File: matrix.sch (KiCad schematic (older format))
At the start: 129 parts

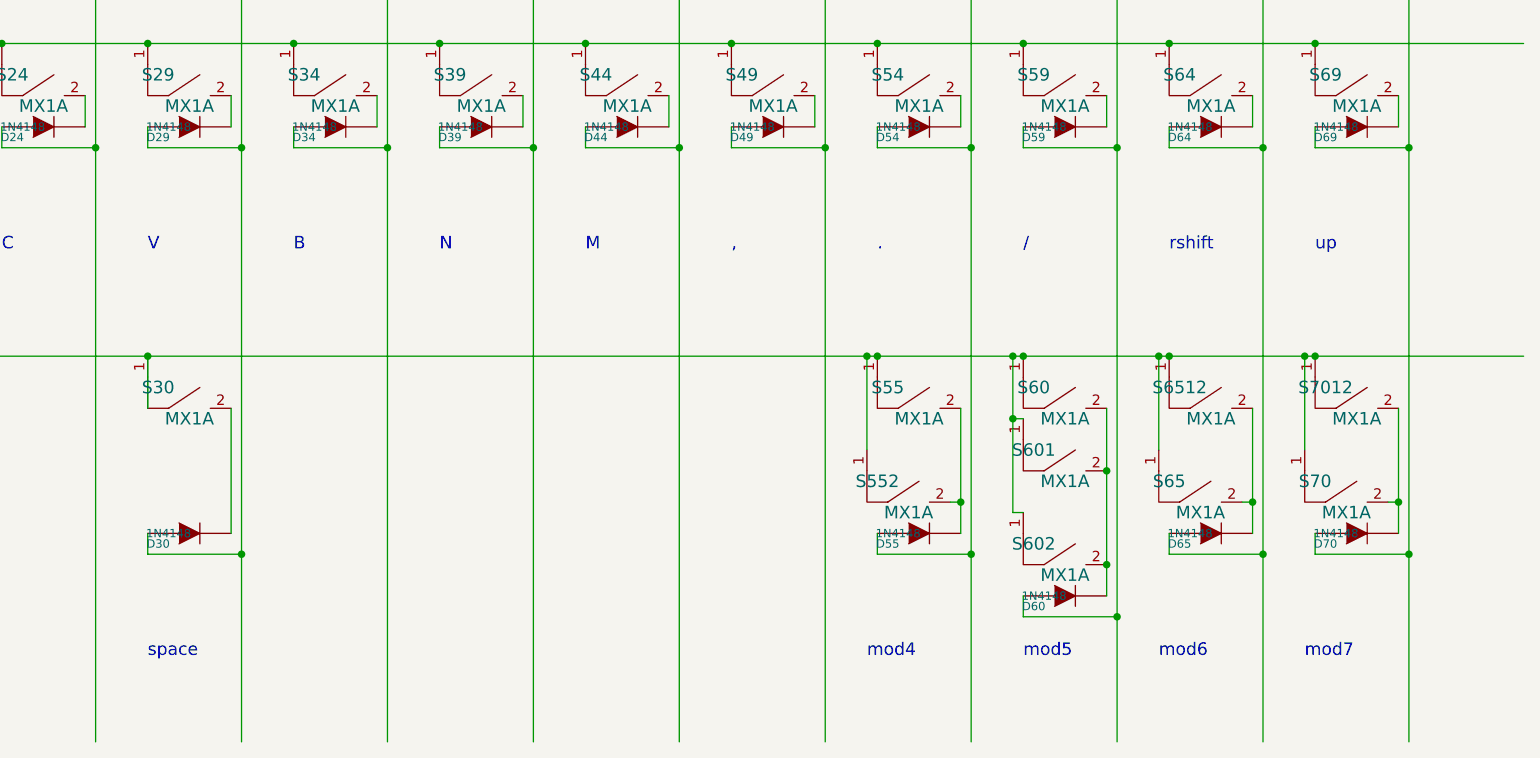
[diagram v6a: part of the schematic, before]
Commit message: New PCB layout for bottom, left, mod4, mod5 and mod6
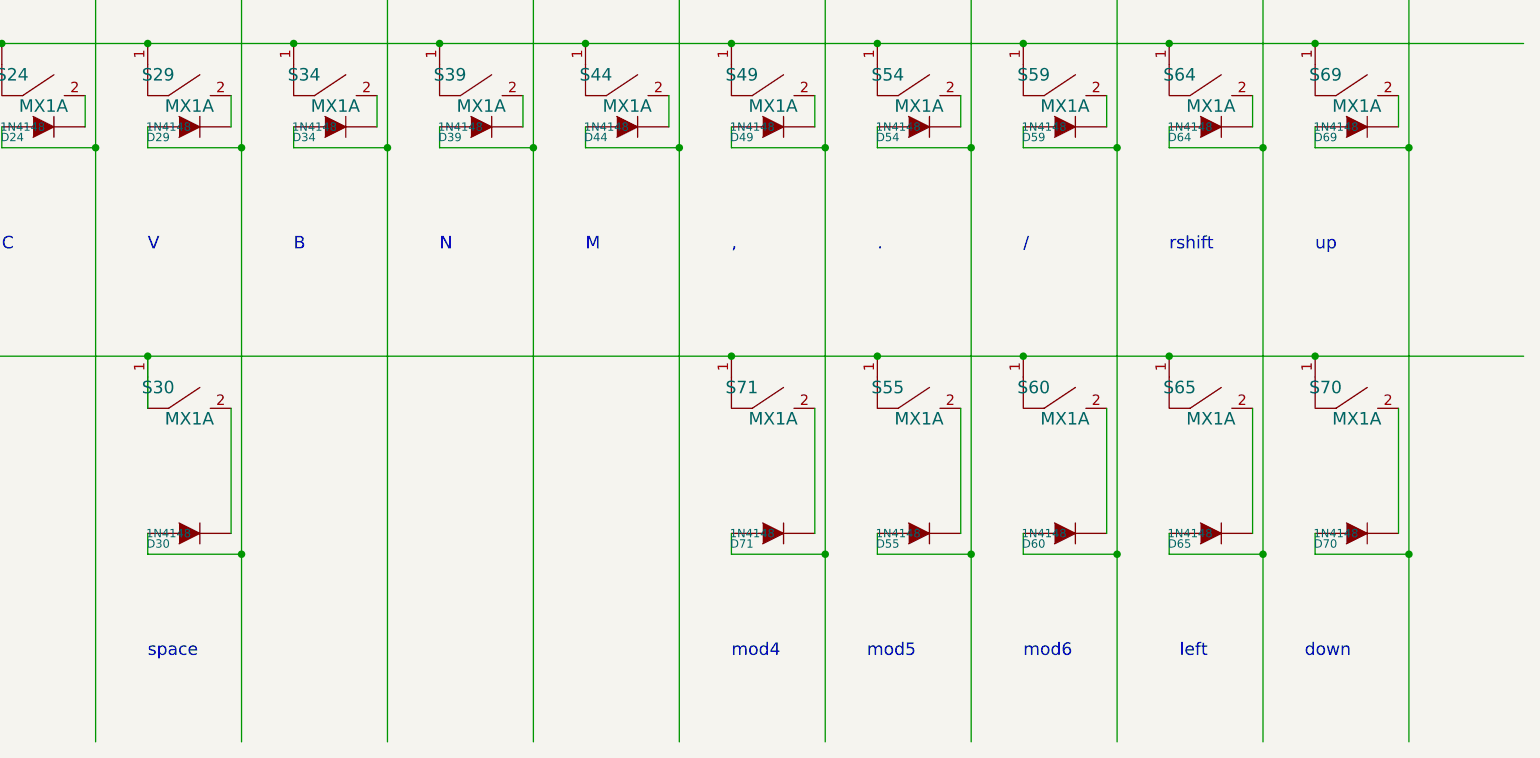
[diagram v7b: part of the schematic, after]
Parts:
- removed S552, S601, S602, S6512, S7012: MX1A, mx1a:MX1A_no3d, symbol mx1a-simple:MX1A
- added D71: 1N4148, 0805:0805D, symbol device:DIODE
- added S71: MX1A, mx1a:MX1A, symbol mx1a-simple:MX1A
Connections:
- wire segments 349 -> 335
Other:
- note added: "down"
- note added: "left"
- note removed: "mod7"
- moved on the sheet: D60, S65, S70
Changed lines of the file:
@@
 L mx1a-simple:MX1A S65
 U 1 1 5040DF5F
-P 11700 9000
-F 0 "S65" H 11550 9250 60  0000 C CNN
-F 1 "MX1A" H 11700 9100 60  0000 C CNN
-F 2 "mx1a:MX1A" H 11700 9000 60  0001 C CNN
-F 3 "" H 11700 9000 60  0001 C CNN
-	1    11700 9000
+P 11750 8550
+F 0 "S65" H 11600 8800 60  0000 C CNN
+F 1 "MX1A" H 11750 8650 60  0000 C CNN
+F 2 "mx1a:MX1A" H 11750 8550 60  0001 C CNN
+F 3 "" H 11750 8550 60  0001 C CNN
+	1    11750 8550
 	1    0    0    -1
 $EndComp
@@
 L mx1a-simple:MX1A S70
 U 1 1 5040DF65
-P 12400 9000
-F 0 "S70" H 12250 9250 60  0000 C CNN
-F 1 "MX1A" H 12400 9100 60  0000 C CNN
-F 2 "mx1a:MX1A" H 12400 9000 60  0001 C CNN
-F 3 "" H 12400 9000 60  0001 C CNN
-	1    12400 9000
-	1    0    0    -1
-$EndComp
-$Comp
-L mx1a-simple:MX1A S552
-U 1 1 5040F08D
-P 10300 9000
-F 0 "S552" H 10150 9250 60  0000 C CNN
-F 1 "MX1A" H 10300 9100 60  0000 C CNN
-F 2 "mx1a:MX1A_no3d" H 10300 9000 60  0001 C CNN
-F 3 "" H 10300 9000 60  0001 C CNN
-	1    10300 9000
-	1    0    0    -1
-$EndComp
-$Comp
-L mx1a-simple:MX1A S602
-U 1 1 5040F09E
-P 11050 9300
-F 0 "S602" H 10900 9550 60  0000 C CNN
-F 1 "MX1A" H 11050 9400 60  0000 C CNN
-F 2 "mx1a:MX1A_no3d" H 11050 9300 60  0001 C CNN
-F 3 "" H 11050 9300 60  0001 C CNN
-	1    11050 9300
-	1    0    0    -1
-$EndComp
-$Comp
-L mx1a-simple:MX1A S6512
-U 1 1 5040F1A3
-P 11750 8550
-F 0 "S6512" H 11600 8800 60  0000 C CNN
-F 1 "MX1A" H 11750 8650 60  0000 C CNN
-F 2 "mx1a:MX1A_no3d" H 11750 8550 60  0001 C CNN
-F 3 "" H 11750 8550 60  0001 C CNN
-	1    11750 8550
-	1    0    0    -1
-$EndComp
-$Comp
-L mx1a-simple:MX1A S7012
-U 1 1 5040F1FA
 P 12450 8550
-F 0 "S7012" H 12300 8800 60  0000 C CNN
+F 0 "S70" H 12300 8800 60  0000 C CNN
 F 1 "MX1A" H 12450 8650 60  0000 C CNN
-F 2 "mx1a:MX1A_no3d" H 12450 8550 60  0001 C CNN
+F 2 "mx1a:MX1A" H 12450 8550 60  0001 C CNN
 F 3 "" H 12450 8550 60  0001 C CNN
 	1    12450 8550
@@
 L device:DIODE D60
 U 1 1 506B59FB
-P 11050 9300
-F 0 "D60" H 10900 9250 40  0000 C CNN
-F 1 "1N4148" H 10950 9300 40  0000 C CNN
-F 2 "0805:0805D" H 11050 9300 60  0001 C CNN
-F 3 "" H 11050 9300 60  0001 C CNN
-F 4 "DC Components" H 5000 5050 60  0001 C CNN "Vendor"
-F 5 "CD4148WS(0805C)" H 5000 5050 60  0001 C CNN "Product"
-F 6 "TME" H 5000 5050 60  0001 C CNN "Supplier"
-F 7 "1N4148-0805" H 5000 5050 60  0001 C CNN "Supplier Symbol"
-	1    11050 9300
+P 11050 9000
+F 0 "D60" H 10900 8950 40  0000 C CNN
+F 1 "1N4148" H 10950 9000 40  0000 C CNN
+F 2 "0805:0805D" H 11050 9000 60  0001 C CNN
+F 3 "" H 11050 9000 60  0001 C CNN
+F 4 "DC Components" H 5000 4750 60  0001 C CNN "Vendor"
+F 5 "CD4148WS(0805C)" H 5000 4750 60  0001 C CNN "Product"
+F 6 "TME" H 5000 4750 60  0001 C CNN "Supplier"
+F 7 "1N4148-0805" H 5000 4750 60  0001 C CNN "Supplier Symbol"
+	1    11050 9000
 	1    0    0    -1
 $EndComp
@@
 F 7 "1N4148-0805" H 3350 3900 60  0001 C CNN "Supplier Symbol"
 	1    3350 5550
-	1    0    0    -1
-$EndComp
-$Comp
-L mx1a-simple:MX1A S601
-U 1 1 5040F098
-P 11050 8850
-F 0 "S601" H 10900 9100 60  0000 C CNN
-F 1 "MX1A" H 11050 8950 60  0000 C CNN
-F 2 "mx1a:MX1A_no3d" H 11050 8850 60  0001 C CNN
-F 3 "" H 11050 8850 60  0001 C CNN
-	1    11050 8850
 	1    0    0    -1
 $EndComp
@@
 mod3
 Text Notes 10100 9600 0    60   ~ 0
-mod4
+mod5
 Text Notes 10850 9600 0    60   ~ 0
-mod5
-Text Notes 11500 9600 0    60   ~ 0
 mod6
+Text Notes 11600 9600 0    60   ~ 0
+left
 Text Notes 12200 9600 0    60   ~ 0
-mod7
+down
 Wire Wire Line
 	4300 1400 4300 3450
 Wire Wire Line
 	3600 1400 3600 3450
-Connection ~ 10100 8150
-Wire Wire Line
-	10100 8150 10100 8600
-Connection ~ 12200 8150
-Wire Wire Line
-	12200 8150 12200 8600
-Connection ~ 10800 8450
-Connection ~ 11500 8150
-Connection ~ 10800 8150
-Wire Wire Line
-	10800 8450 10850 8450
-Wire Wire Line
-	10800 8150 10800 8450
-Wire Wire Line
-	11500 8150 11500 8600
-Connection ~ 12250 8150
-Connection ~ 11550 8150
 Connection ~ 10850 8150
 Connection ~ 10150 8150
@@
 	1800 2950 3150 2950
 Wire Wire Line
-	11250 8400 11250 8700
-Wire Wire Line
-	12650 8400 12650 8850
-Wire Wire Line
-	11950 8400 11950 8850
-Connection ~ 11250 8700
-Wire Wire Line
 	5000 1400 5000 3450
 Wire Wire Line
@@
 	12000 1400 12000 3450
 Wire Wire Line
-	10550 8850 10500 8850
-Wire Wire Line
-	11950 8850 11900 8850
-Wire Wire Line
-	12650 8850 12600 8850
-Wire Wire Line
 	12650 6900 12650 7050
 Wire Wire Line
@@
 Wire Wire Line
 	5650 7050 5650 6900
-Wire Wire Line
-	10550 8400 10550 8850
 Connection ~ 5250 2950
 Connection ~ 5250 4150
@@
 	11550 9100 12000 9100
 Wire Wire Line
-	10850 9300 10850 9400
-Wire Wire Line
-	10850 9400 11300 9400
+	10850 9000 10850 9100
+Wire Wire Line
+	10850 9100 11300 9100
 Wire Wire Line
 	10150 9000 10150 9100
@@
 Wire Wire Line
 	4550 9000 4550 9100
-Connection ~ 12650 8850
-Connection ~ 11950 8850
-Connection ~ 10550 8850
-Connection ~ 11250 9150
 Wire Wire Line
 	3150 5550 3150 5650
@@
 Connection ~ 12700 9100
 Connection ~ 12000 9100
-Connection ~ 11300 9400
 Connection ~ 11300 7150
 Connection ~ 10600 7150
@@
 Connection ~ 9450 2950
 Wire Wire Line
-	10800 8900 10850 8900
-Wire Wire Line
 	12250 3450 12250 3350
 Wire Wire Line
-	10100 8150 10150 8150
-Wire Wire Line
-	12200 8150 12250 8150
-Wire Wire Line
-	10800 8450 10800 8900
-Wire Wire Line
-	11500 8150 11550 8150
-Wire Wire Line
-	10800 8150 10850 8150
-Wire Wire Line
-	12250 8150 13250 8150
-Wire Wire Line
-	11550 8150 12200 8150
-Wire Wire Line
-	10850 8150 11500 8150
-Wire Wire Line
-	10150 8150 10800 8150
-Wire Wire Line
 	12250 6650 13250 6650
 Wire Wire Line
@@
 	3150 2950 3850 2950
 Wire Wire Line
-	11250 8700 11250 9150
-Wire Wire Line
 	5250 2950 5950 2950
 Wire Wire Line
@@
 	9450 6650 10150 6650
 Wire Wire Line
-	12650 8850 12650 9000
-Wire Wire Line
-	11950 8850 11950 9000
-Wire Wire Line
-	10550 8850 10550 9000
-Wire Wire Line
-	11250 9150 11250 9300
-Wire Wire Line
 	3600 3450 3600 4650
 Wire Wire Line
@@
 	12000 9100 12000 10000
 Wire Wire Line
-	11300 9400 11300 10000
-Wire Wire Line
-	11300 7150 11300 9400
+	11300 7150 11300 9100
 Wire Wire Line
 	10600 7150 10600 9100
@@
 	9450 2950 10150 2950
 Wire Wire Line
-	9900 7150 9900 10000
+	9900 7150 9900 9100
 Wire Wire Line
 	12650 3200 12650 3350
@@
 Connection ~ 6650 8150
 Wire Wire Line
-	6650 8150 10100 8150
-Wire Wire Line
 	4550 8150 6650 8150
 Wire Wire Line
@@
 Wire Wire Line
 	11950 6900 11950 7050
+Connection ~ 12250 8150
+Wire Wire Line
+	12250 8150 13250 8150
+Wire Wire Line
+	12650 8400 12650 9000
+Wire Wire Line
+	10850 8150 11550 8150
+Connection ~ 11550 8150
+Wire Wire Line
+	11550 8150 12250 8150
+Wire Wire Line
+	11950 8400 11950 9000
+Wire Wire Line
+	11250 8400 11250 9000
+Wire Wire Line
+	10150 8150 10850 8150
+Connection ~ 11300 9100
+Wire Wire Line
+	11300 9100 11300 10000
+Wire Wire Line
+	6650 8150 9450 8150
+Wire Wire Line
+	10550 8400 10550 9000
+$Comp
+L mx1a-simple:MX1A S71
+U 1 1 620D47D9
+P 9650 8550
+F 0 "S71" H 9500 8800 60  0000 C CNN
+F 1 "MX1A" H 9650 8650 60  0000 C CNN
+F 2 "mx1a:MX1A" H 9650 8550 60  0001 C CNN
+F 3 "" H 9650 8550 60  0001 C CNN
+	1    9650 8550
+	1    0    0    -1
+$EndComp
+$Comp
+L device:DIODE D71
+U 1 1 620F3010
+P 9650 9000
+F 0 "D71" H 9500 8950 40  0000 C CNN
+F 1 "1N4148" H 9550 9000 40  0000 C CNN
+F 2 "0805:0805D" H 9650 9000 60  0001 C CNN
+F 3 "" H 9650 9000 60  0001 C CNN
+F 4 "DC Components" H 4150 5050 60  0001 C CNN "Vendor"
+F 5 "CD4148WS(0805C)" H 4150 5050 60  0001 C CNN "Product"
+F 6 "TME" H 4150 5050 60  0001 C CNN "Supplier"
+F 7 "1N4148-0805" H 4150 5050 60  0001 C CNN "Supplier Symbol"
+	1    9650 9000
+	1    0    0    -1
+$EndComp
+Wire Wire Line
+	9450 9000 9450 9100
+Text Notes 9450 9600 0    60   ~ 0
+mod4
+Wire Wire Line
+	9450 9100 9900 9100
+Connection ~ 9900 9100
+Wire Wire Line
+	9900 9100 9900 10000
+Connection ~ 9450 8150
+Wire Wire Line
+	9450 8150 10150 8150
+Wire Wire Line
+	9850 8400 9850 9000
 $EndSCHEMATC

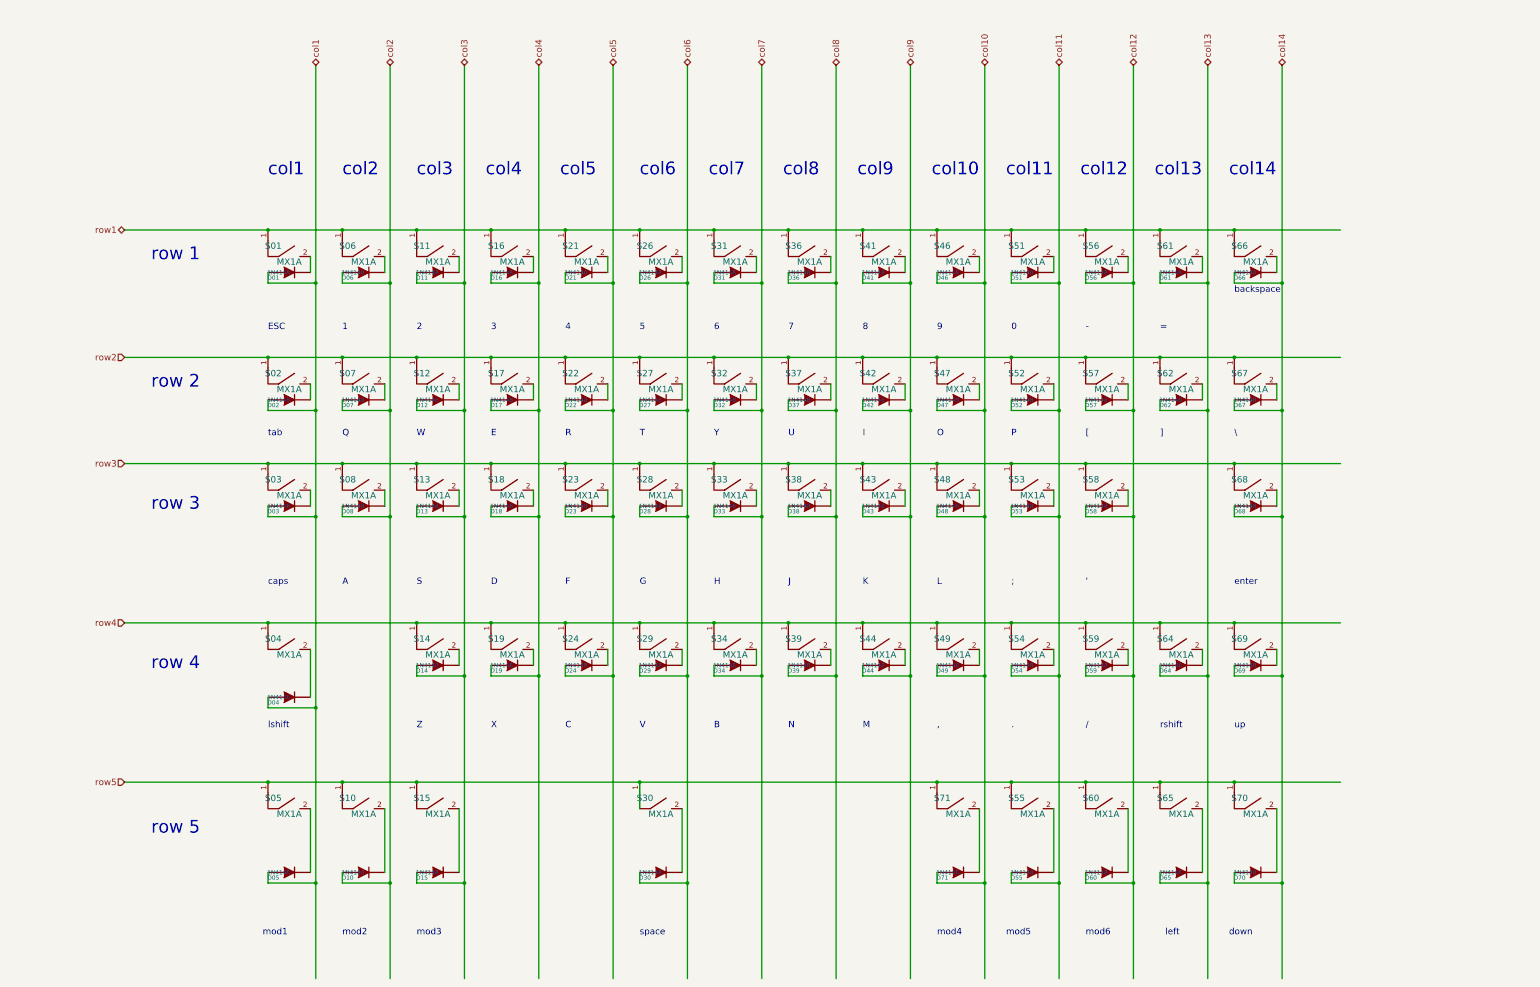
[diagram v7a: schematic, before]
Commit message: Add numpad cols to schematic
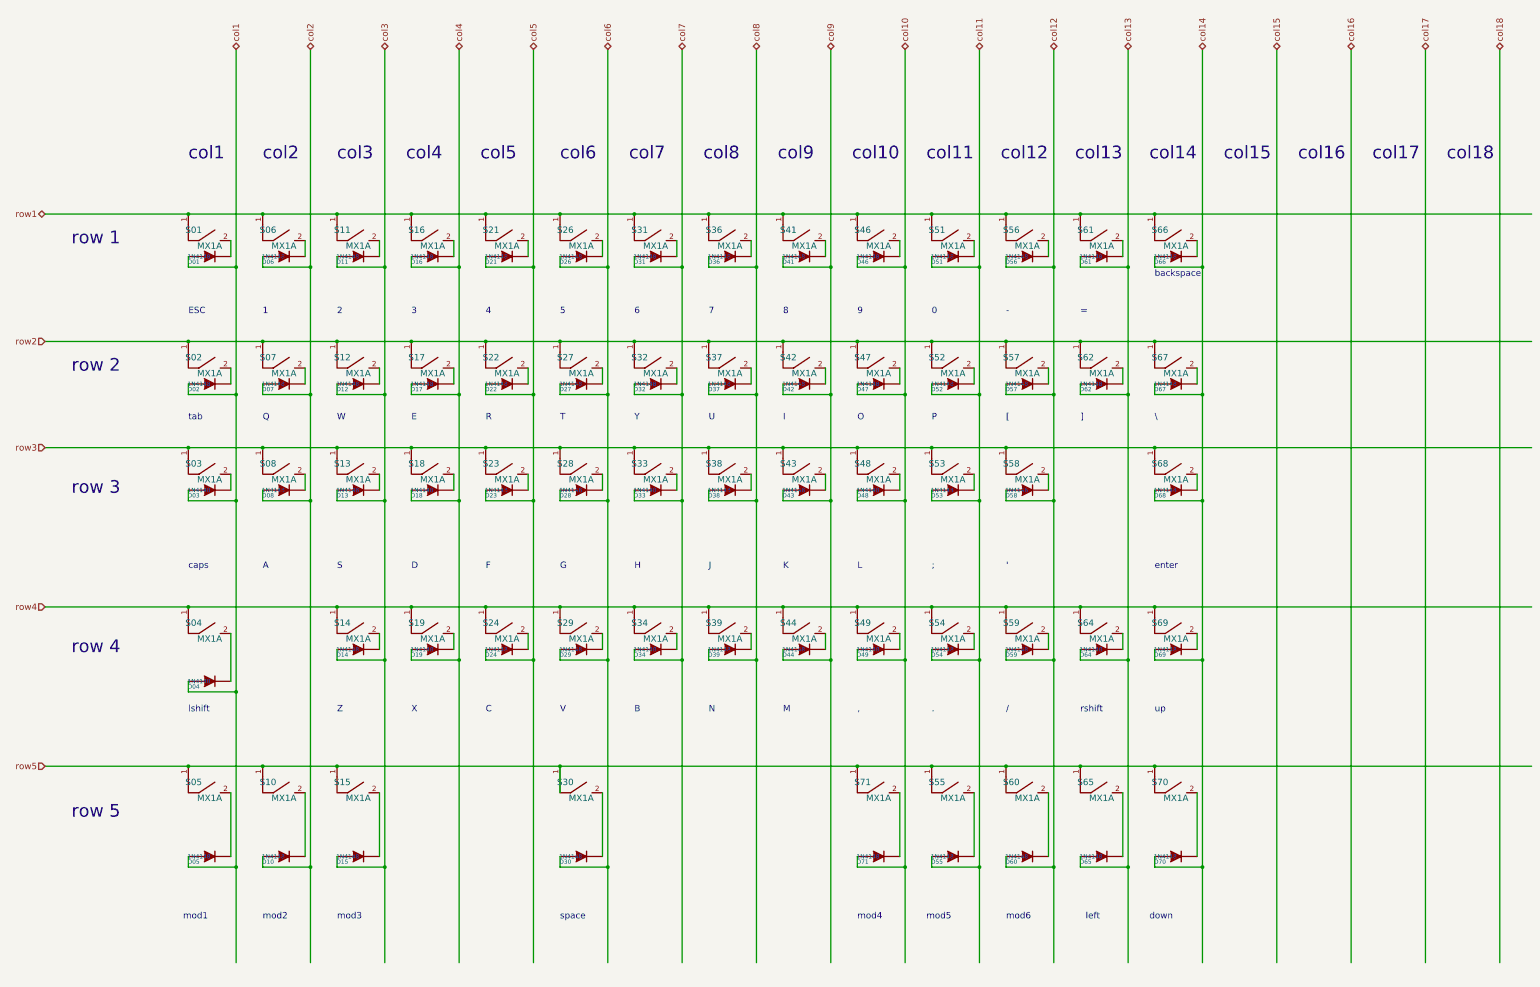
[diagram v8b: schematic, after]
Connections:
- net labels added: col15, col16, col17, col18
- wire segments 335 -> 339
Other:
- note added: "col15"
- note added: "col16"
- note added: "col17"
- note added: "col18"
- moved on the sheet: D01, D02, D03, D04, D05, D06, D07, D08, D10, D11, D12, D13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
